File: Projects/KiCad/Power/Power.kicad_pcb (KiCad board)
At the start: 2 copper layers, 110 x 95 mm, 50 parts, among them J1 Conn_01x02_Pin, J2 Conn_01x02_Pin, J3 Conn_01x02_Pin, J4 Conn_01x02_Pin, Q1 TJ8S06M3L, Q2 TJ8S06M3L, Q3 TJ8S06M3L, SW2 SW_SPDT, U1 NJM7812SDL1, U2 NJM7812SDL1, U3 NJM7812SDL1, U4 LTC4416EMS#PBF

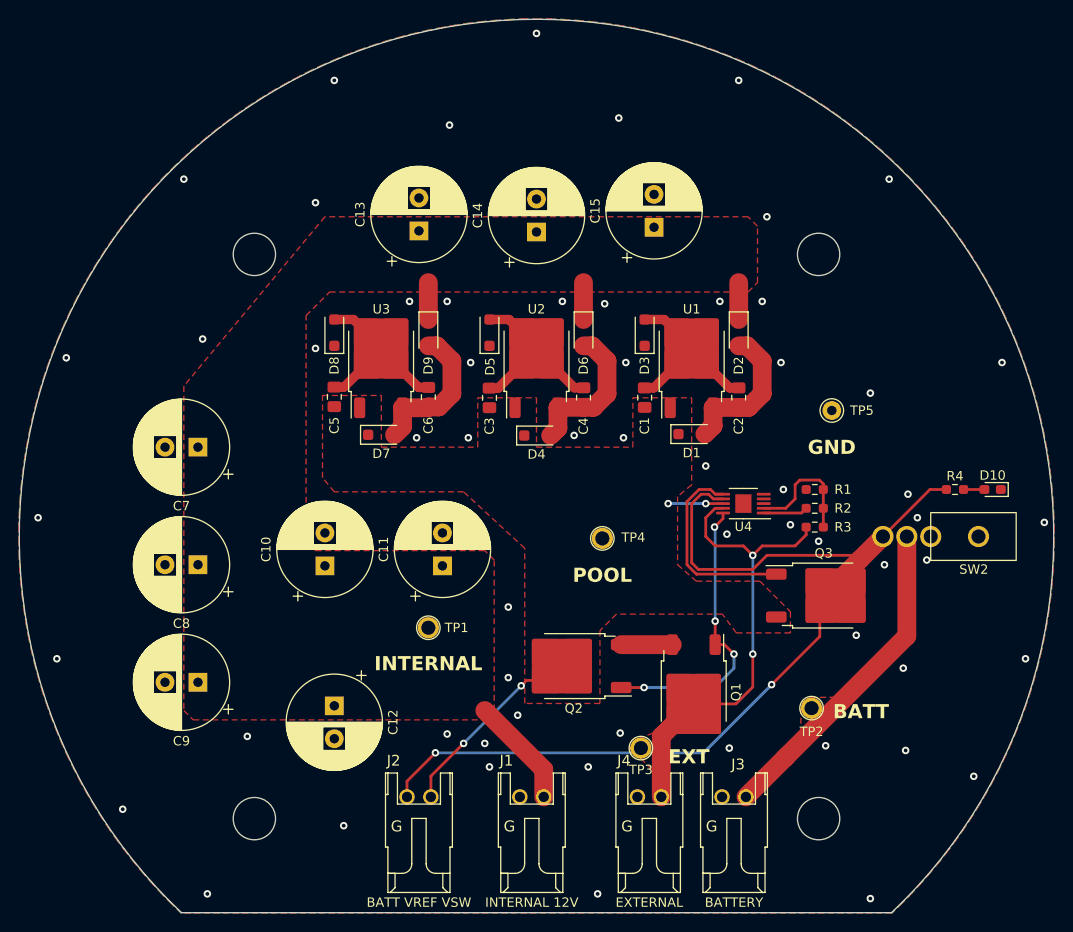
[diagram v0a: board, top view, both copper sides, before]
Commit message: STEPファイルを再生成
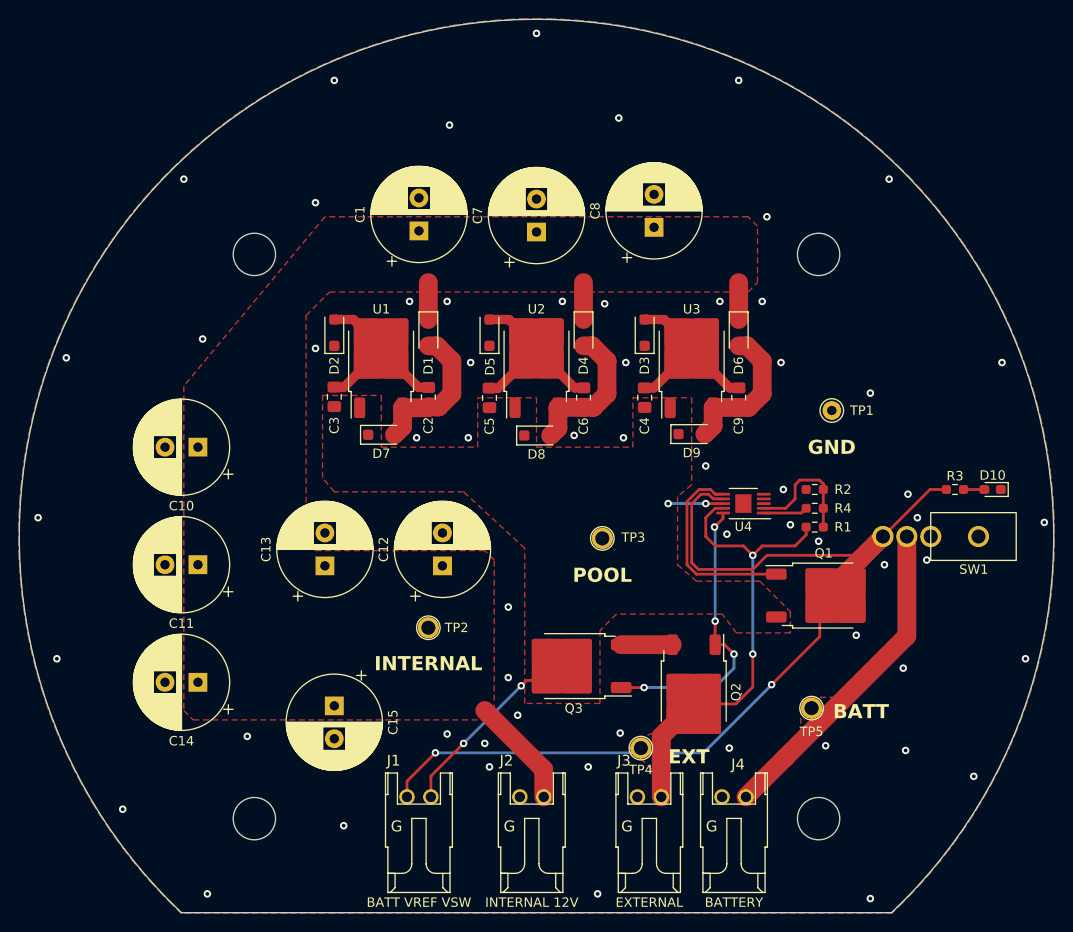
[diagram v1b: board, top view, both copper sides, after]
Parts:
- renumbered C13 to C1, C7 to C10, C8 to C11, C11 to C12, C10 to C13, C9 to C14, C12 to C15, C6 to C2, C5 to C3, C1 to C4, C3 to C5, C4 to C6, C14 to C7, C15 to C8, C2 to C9, D9 to D1, D8 to D2, D6 to D4, D2 to D6, D4 to D8, D1 to D9, J2 to J1, J1 to J2, J4 to J3, J3 to J4, Q3 to Q1, Q1 to Q2, Q2 to Q3, R3 to R1, R1 to R2, R4 to R3, R2 to R4, SW2 to SW1, TP5 to TP1, TP1 to TP2, TP4 to TP3, TP3 to TP4, TP2 to TP5, U3 to U1, U1 to U3

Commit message: 変圧基板の値を修正
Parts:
- C1, C10, C11, C12, C13, C14, C15, C7, C8: value C -> 270μF
- R4: value 70kΩ -> 68kΩ
